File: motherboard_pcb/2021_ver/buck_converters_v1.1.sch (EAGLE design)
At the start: 127 parts, among them J1 D15S24A4GV00LF, J4 171-025-213R001, Q1 IRFR5305, U2 TPS54302, U3 TPS54302, X5 332-02

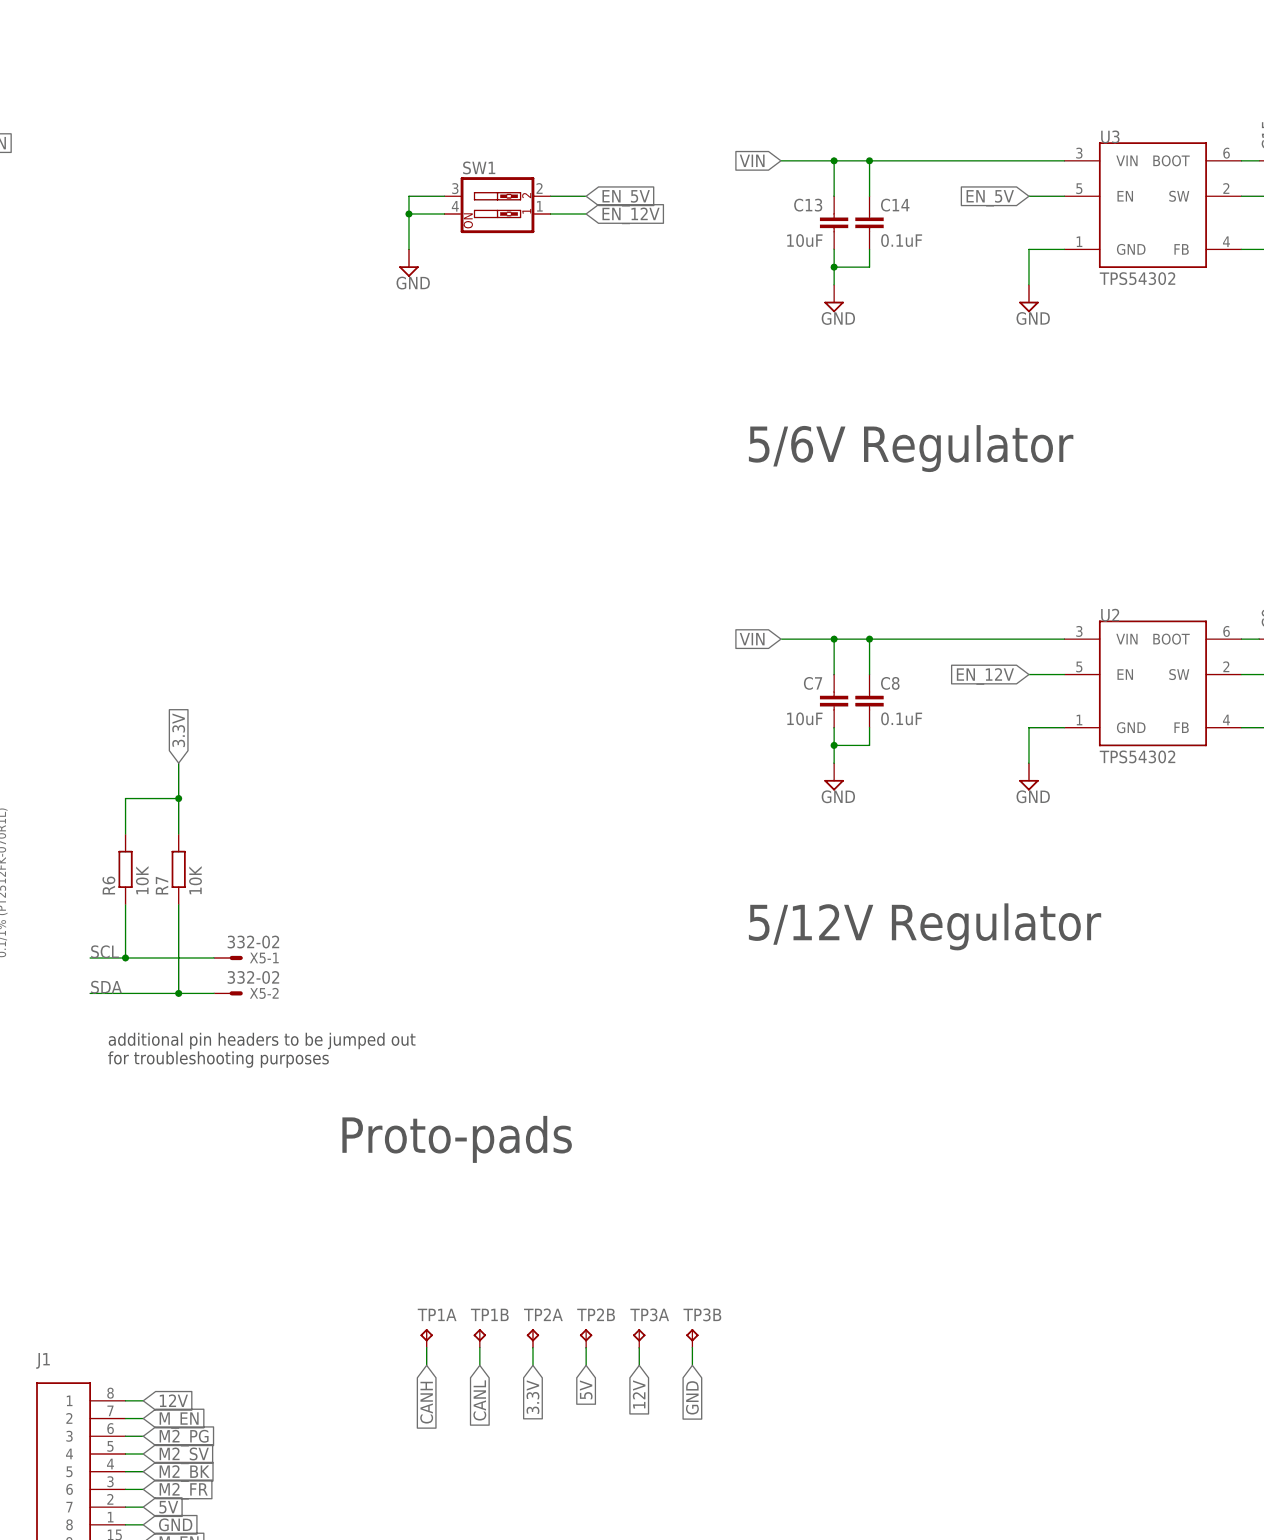
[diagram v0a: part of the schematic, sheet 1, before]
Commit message: modified for silkscreen and 12V converter
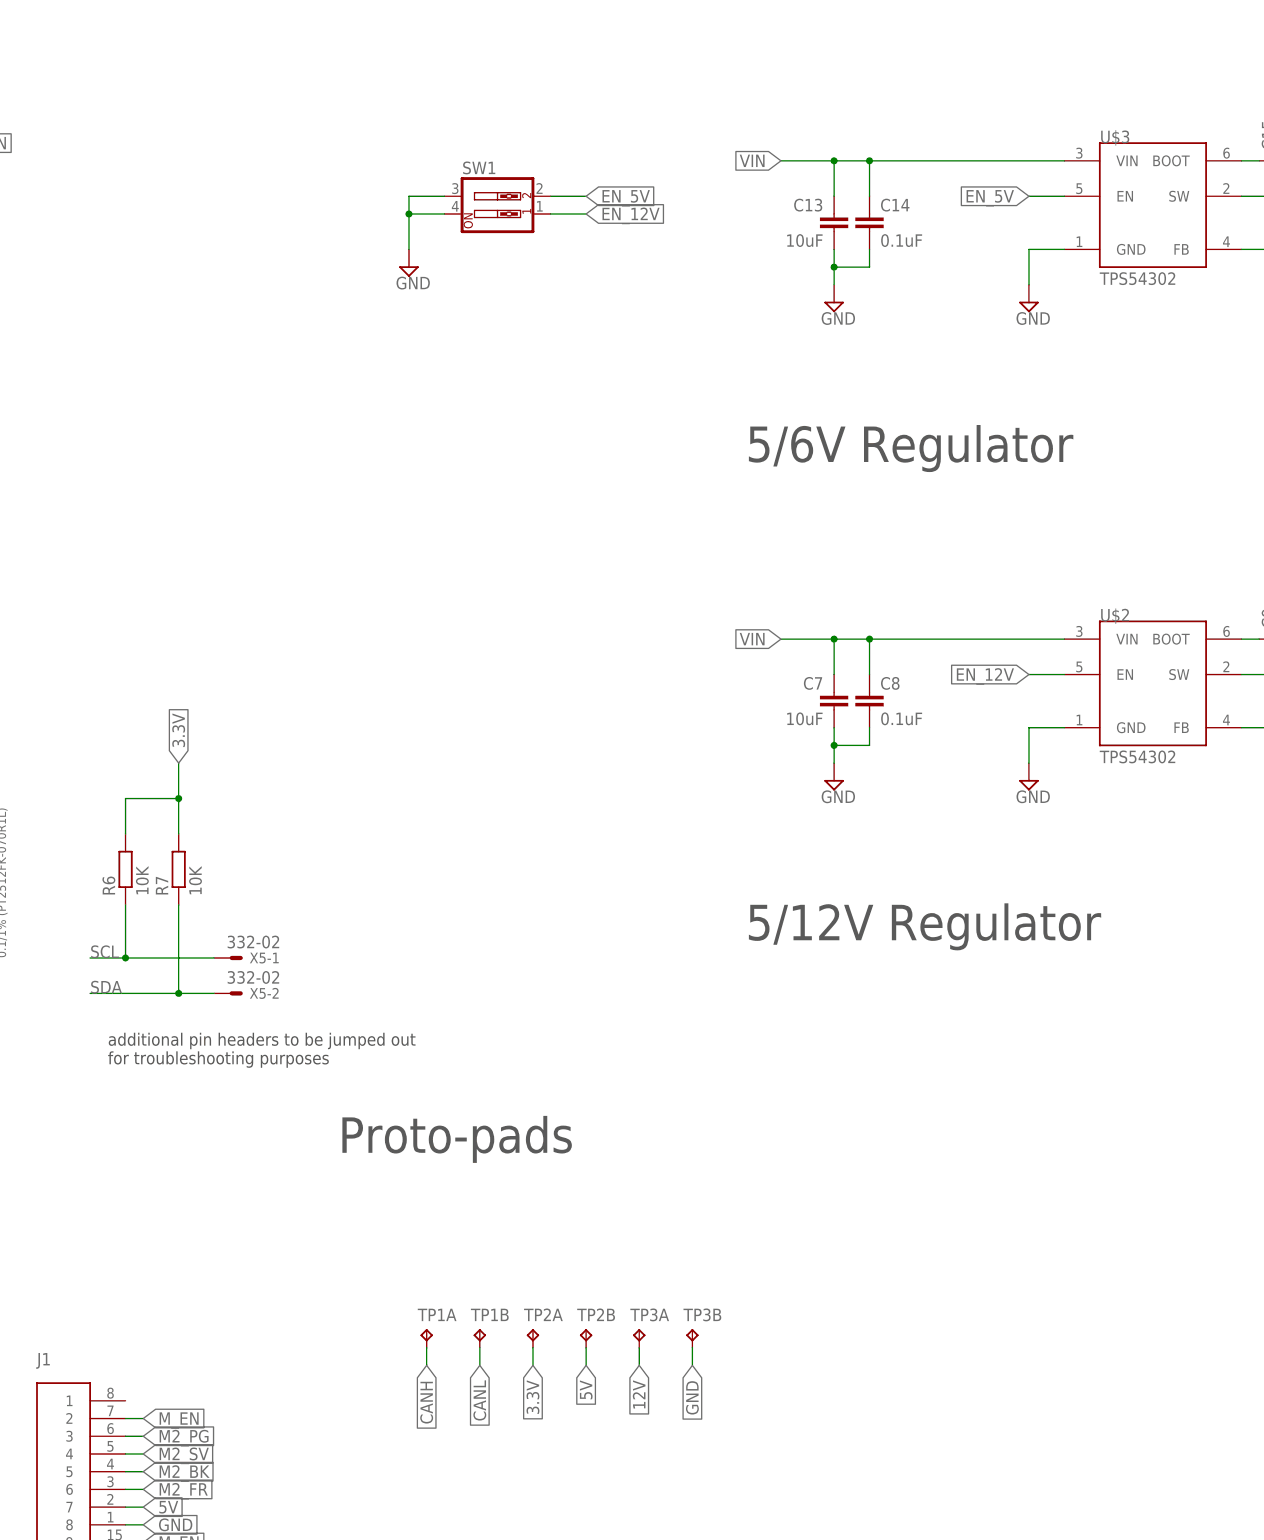
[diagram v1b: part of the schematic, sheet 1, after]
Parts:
- renumbered U2 to U$2, U3 to U$3
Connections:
- net 12V: no longer J1.1
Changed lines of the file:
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@@
 </classes>
 <parts>
-<part name="U2" library="TPSxxxxxx-buck-regulators" deviceset="TPS54302" device=""/>
+<part name="U$2" library="TPSxxxxxx-buck-regulators" deviceset="TPS54302" device=""/>
 <part name="C7" library="rcl" library_urn="urn:adsk.eagle:library:334" deviceset="C-EU" device="C0805" package3d_urn="urn:adsk.eagle:package:23617/2" value="10uF"/>
 <part name="C8" library="rcl" library_urn="urn:adsk.eagle:library:334" deviceset="C-EU" device="C0805" package3d_urn="urn:adsk.eagle:package:23617/2" value="0.1uF"/>
@@
 <part name="SUPPLY7" library="supply2" library_urn="urn:adsk.eagle:library:372" deviceset="GND" device=""/>
 <part name="SUPPLY8" library="supply2" library_urn="urn:adsk.eagle:library:372" deviceset="GND" device=""/>
-<part name="U3" library="TPSxxxxxx-buck-regulators" deviceset="TPS54302" device=""/>
+<part name="U$3" library="TPSxxxxxx-buck-regulators" deviceset="TPS54302" device=""/>
 <part name="C13" library="rcl" library_urn="urn:adsk.eagle:library:334" deviceset="C-EU" device="C0805" package3d_urn="urn:adsk.eagle:package:23617/2" value="10uF"/>
 <part name="C14" library="rcl" library_urn="urn:adsk.eagle:library:334" deviceset="C-EU" device="C0805" package3d_urn="urn:adsk.eagle:package:23617/2" value="0.1uF"/>
@@
 </plain>
 <instances>
-<instance part="U2" gate="G$1" x="302.26" y="170.18" smashed="yes">
+<instance part="U$2" gate="G$1" x="302.26" y="170.18" smashed="yes">
 <attribute name="NAME" x="294.64" y="177.8" size="1.778" layer="95"/>
 <attribute name="VALUE" x="294.64" y="157.48" size="1.778" layer="96"/>
@@
 <attribute name="VALUE" x="363.855" y="118.745" size="1.778" layer="96"/>
 </instance>
-<instance part="U3" gate="G$1" x="302.26" y="238.76" smashed="yes">
+<instance part="U$3" gate="G$1" x="302.26" y="238.76" smashed="yes">
 <attribute name="NAME" x="294.64" y="246.38" size="1.778" layer="95"/>
 <attribute name="VALUE" x="294.64" y="226.06" size="1.778" layer="96"/>
@@
 </segment>
 <segment>
-<pinref part="U2" gate="G$1" pin="GND"/>
+<pinref part="U$2" gate="G$1" pin="GND"/>
 <wire x1="289.56" y1="162.56" x2="284.48" y2="162.56" width="0.1524" layer="91"/>
 <pinref part="SUPPLY5" gate="GND" pin="GND"/>
@@
 <pinref part="SUPPLY9" gate="GND" pin="GND"/>
 <wire x1="284.48" y1="226.06" x2="284.48" y2="231.14" width="0.1524" layer="91"/>
-<pinref part="U3" gate="G$1" pin="GND"/>
+<pinref part="U$3" gate="G$1" pin="GND"/>
 <wire x1="284.48" y1="231.14" x2="289.56" y2="231.14" width="0.1524" layer="91"/>
 </segment>
@@
 <net name="VIN" class="0">
 <segment>
-<pinref part="U2" gate="G$1" pin="VIN"/>
+<pinref part="U$2" gate="G$1" pin="VIN"/>
 <wire x1="289.56" y1="175.26" x2="261.62" y2="175.26" width="0.1524" layer="91"/>
 <pinref part="C7" gate="G$1" pin="1"/>
@@
 </segment>
 <segment>
-<pinref part="U3" gate="G$1" pin="VIN"/>
+<pinref part="U$3" gate="G$1" pin="VIN"/>
 <wire x1="289.56" y1="243.84" x2="261.62" y2="243.84" width="0.1524" layer="91"/>
 <pinref part="C13" gate="G$1" pin="1"/>
@@
 <wire x1="360.68" y1="139.7" x2="365.76" y2="139.7" width="0.1524" layer="91"/>
 <junction x="365.76" y="139.7"/>
-<pinref part="U2" gate="G$1" pin="FB"/>
+<pinref part="U$2" gate="G$1" pin="FB"/>
 <wire x1="314.96" y1="162.56" x2="335.28" y2="162.56" width="0.1524" layer="91"/>
 <wire x1="335.28" y1="162.56" x2="335.28" y2="139.7" width="0.1524" layer="91"/>
@@
 <net name="N$9" class="0">
 <segment>
-<pinref part="U2" gate="G$1" pin="BOOT"/>
+<pinref part="U$2" gate="G$1" pin="BOOT"/>
 <pinref part="C9" gate="G$1" pin="1"/>
 <wire x1="314.96" y1="175.26" x2="317.5" y2="175.26" width="0.1524" layer="91"/>
@@
 <pinref part="L2" gate="G$1" pin="1"/>
 <wire x1="327.66" y1="170.18" x2="330.2" y2="170.18" width="0.1524" layer="91"/>
-<pinref part="U2" gate="G$1" pin="SW"/>
+<pinref part="U$2" gate="G$1" pin="SW"/>
 <wire x1="314.96" y1="170.18" x2="327.66" y2="170.18" width="0.1524" layer="91"/>
 <junction x="327.66" y="170.18"/>
@@
 <wire x1="360.68" y1="208.28" x2="365.76" y2="208.28" width="0.1524" layer="91"/>
 <junction x="365.76" y="208.28"/>
-<pinref part="U3" gate="G$1" pin="FB"/>
+<pinref part="U$3" gate="G$1" pin="FB"/>
 <wire x1="314.96" y1="231.14" x2="335.28" y2="231.14" width="0.1524" layer="91"/>
 <wire x1="335.28" y1="231.14" x2="335.28" y2="208.28" width="0.1524" layer="91"/>
@@
 <net name="N$14" class="0">
 <segment>
-<pinref part="U3" gate="G$1" pin="BOOT"/>
+<pinref part="U$3" gate="G$1" pin="BOOT"/>
 <pinref part="C15" gate="G$1" pin="1"/>
 <wire x1="314.96" y1="243.84" x2="317.5" y2="243.84" width="0.1524" layer="91"/>
@@
 <pinref part="L3" gate="G$1" pin="1"/>
 <wire x1="327.66" y1="238.76" x2="330.2" y2="238.76" width="0.1524" layer="91"/>
-<pinref part="U3" gate="G$1" pin="SW"/>
+<pinref part="U$3" gate="G$1" pin="SW"/>
 <wire x1="314.96" y1="238.76" x2="327.66" y2="238.76" width="0.1524" layer="91"/>
 <junction x="327.66" y="238.76"/>
@@
 <label x="228.6" y="71.12" size="1.778" layer="95" rot="R270" xref="yes"/>
 </segment>
-<segment>
-<pinref part="J1" gate="G$1" pin="1"/>
-<wire x1="154.94" y1="66.04" x2="157.48" y2="66.04" width="0.1524" layer="91"/>
-<label x="157.48" y="66.04" size="1.778" layer="95" xref="yes"/>
-</segment>
 </net>
 <net name="EN_12V" class="0">
 <segment>
-<pinref part="U2" gate="G$1" pin="EN"/>
+<pinref part="U$2" gate="G$1" pin="EN"/>
 <wire x1="289.56" y1="170.18" x2="284.48" y2="170.18" width="0.1524" layer="91"/>
 <label x="284.48" y="170.18" size="1.778" layer="95" rot="R180" xref="yes"/>
@@
 <net name="EN_5V" class="0">
 <segment>
-<pinref part="U3" gate="G$1" pin="EN"/>
+<pinref part="U$3" gate="G$1" pin="EN"/>
 <wire x1="289.56" y1="238.76" x2="284.48" y2="238.76" width="0.1524" layer="91"/>
 <label x="284.48" y="238.76" size="1.778" layer="95" rot="R180" xref="yes"/>
